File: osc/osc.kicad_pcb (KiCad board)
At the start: 2 copper layers, 25.4 x 25.4 mm, 18 parts, among them P1 CONN_1, P2 CONN_1, P3 CONN_1, P4 CONN_1, P5 CONN_1, P6 CONN_5X2, Y4 M100

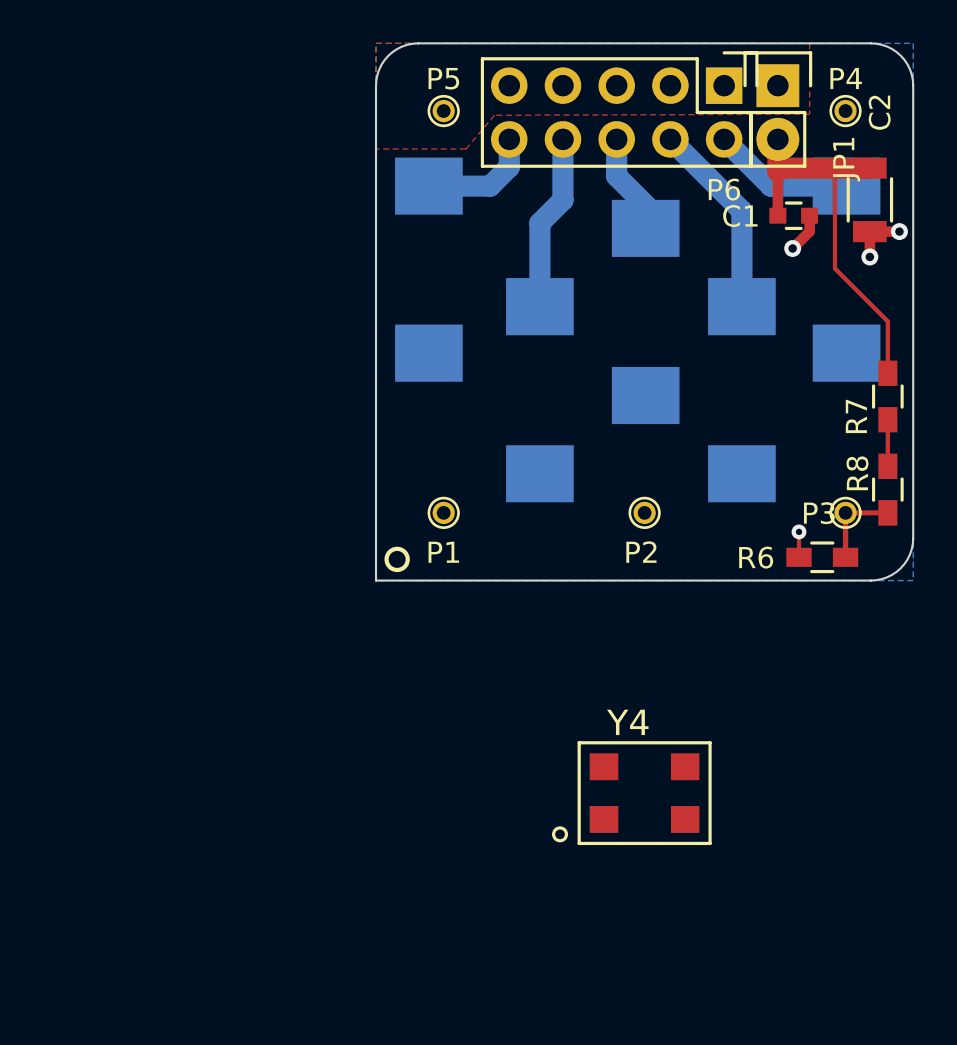
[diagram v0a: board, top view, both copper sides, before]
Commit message: Add Y3 footprint: SMT XO 7.0 x 5.0 mm
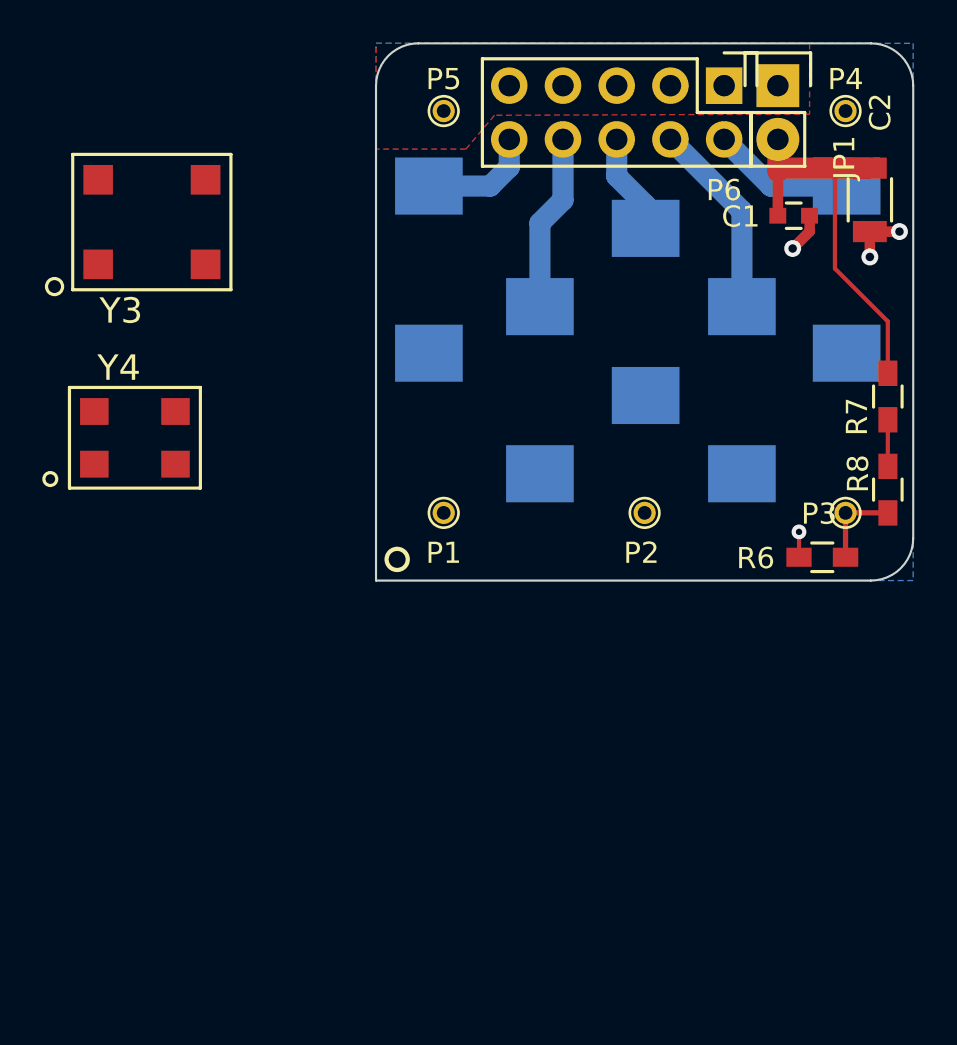
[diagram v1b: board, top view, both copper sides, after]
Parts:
- added Y3: AST3TQ-28, footprints:OSC7050, F.Cu at (89.4, 83.0)
- moved Y4 29.4 mm to (88.6, 93.2)
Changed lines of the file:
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@@
 (kicad_pcb (version 4) (host pcbnew 4.0.2-stable)
   (general
-    (links 29)
-    (no_connects 18)
-    (area 99.949999 74.549999 125.450001 100.050001)
+    (links 33)
+    (no_connects 22)
+    (area 84.070861 74.549999 127.025 101.725)
     (thickness 1.6)
     (drawings 8)
     (tracks 34)
     (zones 0)
-    (modules 18)
+    (modules 19)
     (nets 13)
   )
@@
       (effects (font (size 1 1) (thickness 0.1)))
     )
-    (fp_text value 0 (at 0 1.9 90) (layer F.Fab)
+    (fp_text value 0 (at 0 1.9 90) (layer F.Fab) hide
       (effects (font (size 1 1) (thickness 0.15)))
     )
@@
   )
   (module footprints:OSC5032 (layer F.Cu)
-    (at 112.7 110.050001)
+    (at 88.6 93.25)
     (fp_text reference Y4 (at -0.75 -3.3 180) (layer F.SilkS)
       (effects (font (size 1.2 1.2) (thickness 0.15)))
@@
       (net 2 /GND))
   )
+  (module footprints:OSC7050 (layer F.Cu)
+    (at 89.4 83.05)
+    (fp_text reference Y3 (at -1.45 4.2 180) (layer F.SilkS)
+      (effects (font (size 1.2 1.2) (thickness 0.15)))
+    )
+    (fp_text value AST3TQ-28 (at 0 0) (layer F.Fab)
+      (effects (font (size 1.2 1.2) (thickness 0.15)))
+    )
+    (fp_circle (center -4.6 3.05) (end -4.25 3.2) (layer F.SilkS) (width 0.15))
+    (fp_line (start -3.74 -3.2) (end -3.74 3.2) (layer F.SilkS) (width 0.15))
+    (fp_line (start -3.74 3.2) (end 3.74 3.2) (layer F.SilkS) (width 0.15))
+    (fp_line (start 3.74 3.2) (end 3.74 -3.2) (layer F.SilkS) (width 0.15))
+    (fp_line (start 3.74 -3.2) (end -3.74 -3.2) (layer F.SilkS) (width 0.15))
+    (pad 4 smd rect (at -2.54 -2) (size 1.4 1.4) (layers F.Cu F.Paste F.Mask)
+      (net 1 /Vdd))
+    (pad 1 smd rect (at -2.54 2) (size 1.4 1.4) (layers F.Cu F.Paste F.Mask)
+      (net 12 /Vc))
+    (pad 3 smd rect (at 2.54 -2) (size 1.4 1.4) (layers F.Cu F.Paste F.Mask)
+      (net 4 /Fout))
+    (pad 2 smd rect (at 2.54 2) (size 1.4 1.4) (layers F.Cu F.Paste F.Mask)
+      (net 2 /GND))
+  )

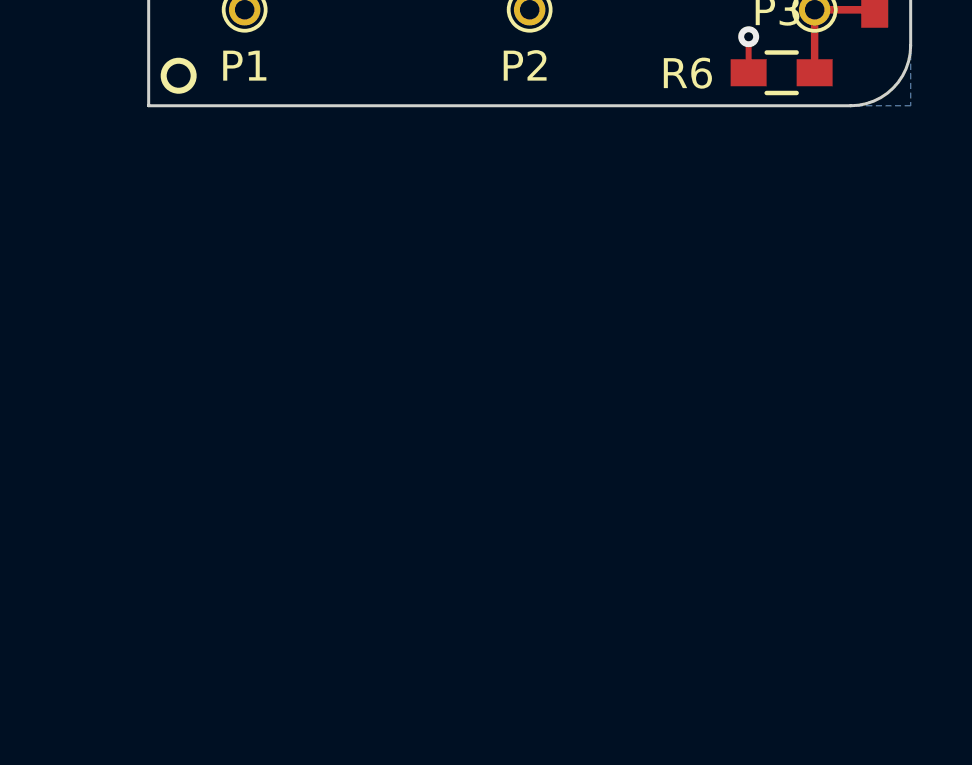
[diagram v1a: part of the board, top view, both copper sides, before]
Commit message: All footprints are created and added to the schematic and the board.
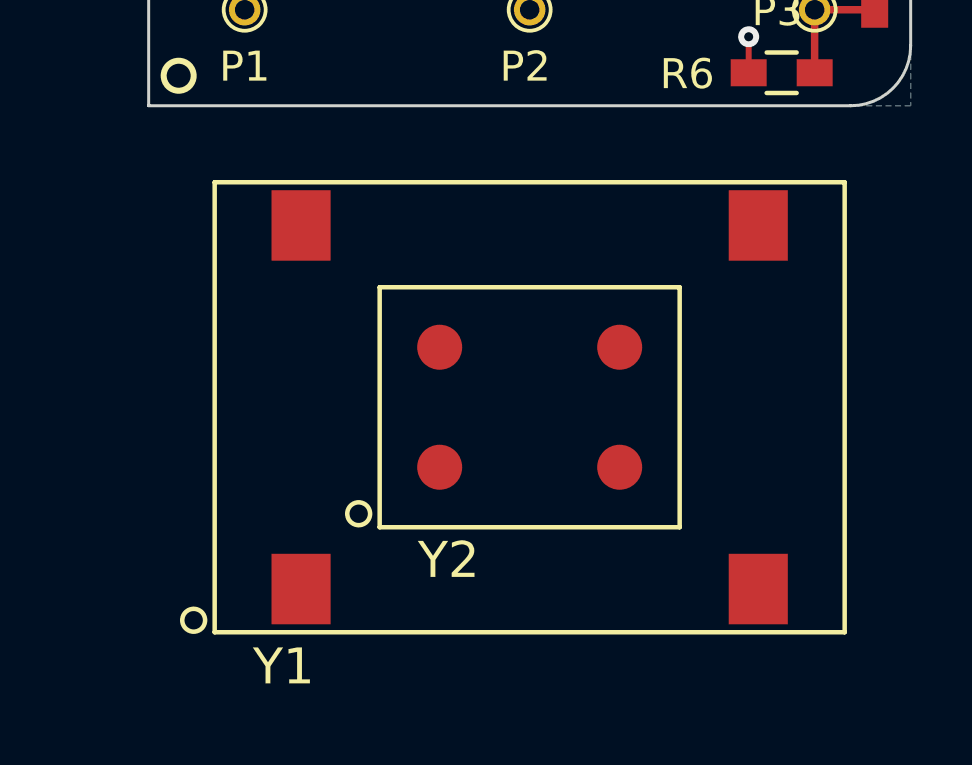
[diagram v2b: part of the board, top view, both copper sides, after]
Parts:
- added Y1: ASOF3S3, footprints:OSC-ASOF3S3, F.Cu at (112.7, 110.1)
- added Y2: AOCJYR, footprints:OSC-AOCJYR-SMT, F.Cu at (112.7, 110.1)
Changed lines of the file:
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@@
 (kicad_pcb (version 4) (host pcbnew 4.0.2-stable)
   (general
-    (links 33)
-    (no_connects 22)
-    (area 84.070861 74.549999 127.025 101.725)
+    (links 41)
+    (no_connects 30)
+    (area 84.070861 74.549999 127.025 119.765001)
     (thickness 1.6)
     (drawings 8)
     (tracks 34)
     (zones 0)
-    (modules 19)
+    (modules 21)
     (nets 13)
   )
@@
       (net 2 /GND))
   )
+  (module footprints:OSC-ASOF3S3 (layer F.Cu)
+    (at 112.7 110.050001)
+    (fp_text reference Y1 (at -8.2 8.65 180) (layer F.SilkS)
+      (effects (font (size 1.2 1.2) (thickness 0.15)))
+    )
+    (fp_text value ASOF3S3 (at 0 0) (layer F.Fab)
+      (effects (font (size 1.2 1.2) (thickness 0.15)))
+    )
+    (fp_circle (center -11.2 7.1) (end -10.85 7.25) (layer F.SilkS) (width 0.15))
+    (fp_line (start -10.5 -7.5) (end -10.5 7.5) (layer F.SilkS) (width 0.15))
+    (fp_line (start -10.5 7.5) (end 10.5 7.5) (layer F.SilkS) (width 0.15))
+    (fp_line (start 10.5 7.5) (end 10.5 -7.5) (layer F.SilkS) (width 0.15))
+    (fp_line (start 10.5 -7.5) (end -10.5 -7.5) (layer F.SilkS) (width 0.15))
+    (pad 14 smd rect (at -7.62 -6.06) (size 1.97 2.35) (layers F.Cu F.Paste F.Mask)
+      (net 1 /Vdd))
+    (pad 1 smd rect (at -7.62 6.06) (size 1.97 2.35) (layers F.Cu F.Paste F.Mask)
+      (net 12 /Vc))
+    (pad 8 smd rect (at 7.62 -6.06) (size 1.97 2.35) (layers F.Cu F.Paste F.Mask)
+      (net 4 /Fout))
+    (pad 7 smd rect (at 7.62 6.06) (size 1.97 2.35) (layers F.Cu F.Paste F.Mask)
+      (net 2 /GND))
+  )
+  (module footprints:OSC-AOCJYR-SMT (layer F.Cu)
+    (at 112.7 110.050001)
+    (fp_text reference Y2 (at -2.7 5.1) (layer F.SilkS)
+      (effects (font (size 1.2 1.2) (thickness 0.15)))
+    )
+    (fp_text value AOCJYR (at 0 0) (layer F.Fab)
+      (effects (font (size 1.2 1.2) (thickness 0.15)))
+    )
+    (fp_circle (center -5.7 3.55) (end -5.35 3.7) (layer F.SilkS) (width 0.15))
+    (fp_line (start -5 -4) (end -5 4) (layer F.SilkS) (width 0.15))
+    (fp_line (start -5 4) (end 5 4) (layer F.SilkS) (width 0.15))
+    (fp_line (start 5 4) (end 5 -4) (layer F.SilkS) (width 0.15))
+    (fp_line (start 5 -4) (end -5 -4) (layer F.SilkS) (width 0.15))
+    (pad 4 smd circle (at -3 -2) (size 1.5 1.5) (layers F.Cu F.Paste F.Mask)
+      (net 1 /Vdd))
+    (pad 1 smd circle (at -3 2) (size 1.5 1.5) (layers F.Cu F.Paste F.Mask)
+      (net 12 /Vc))
+    (pad 3 smd circle (at 3 -2) (size 1.5 1.5) (layers F.Cu F.Paste F.Mask)
+      (net 4 /Fout))
+    (pad 2 smd circle (at 3 2) (size 1.5 1.5) (layers F.Cu F.Paste F.Mask)
+      (net 2 /GND))
+  )

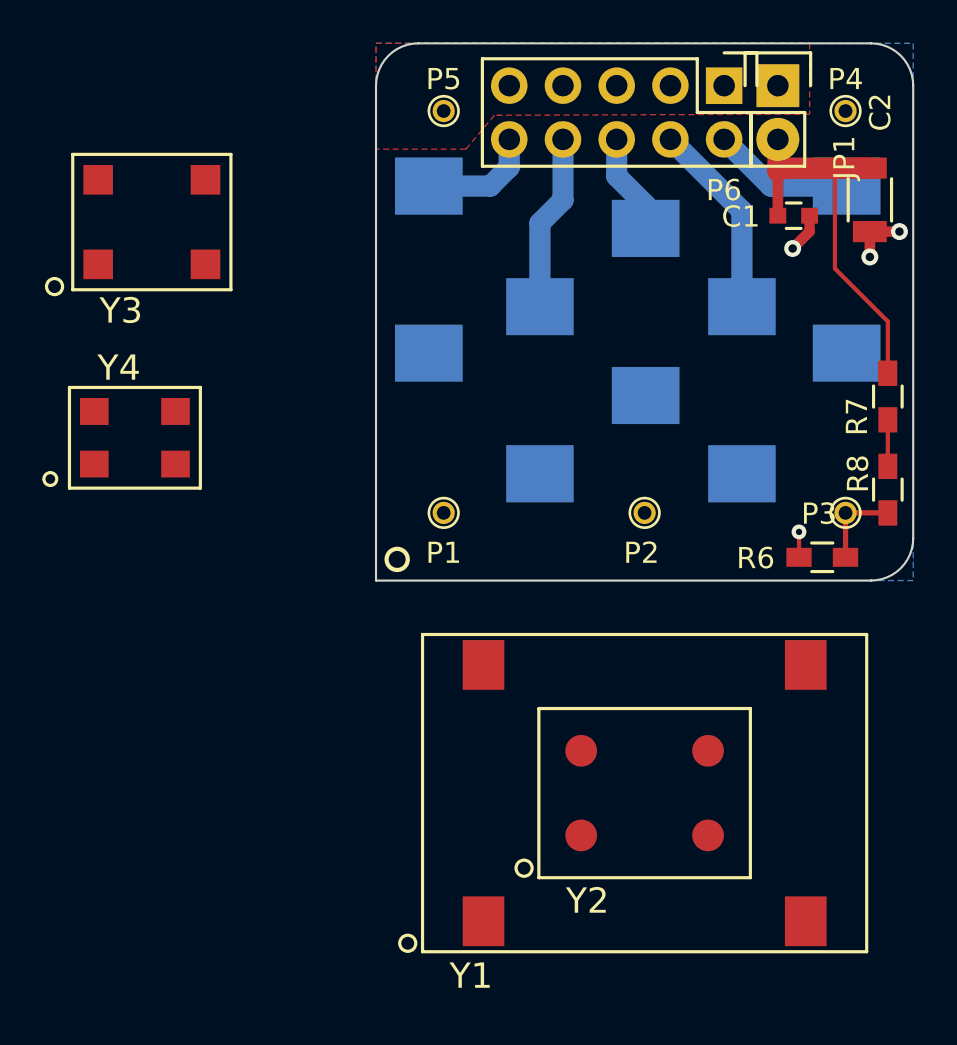
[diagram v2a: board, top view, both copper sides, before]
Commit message: Add an extra .1uF cap (build-time option, depends on the Osc assembled)
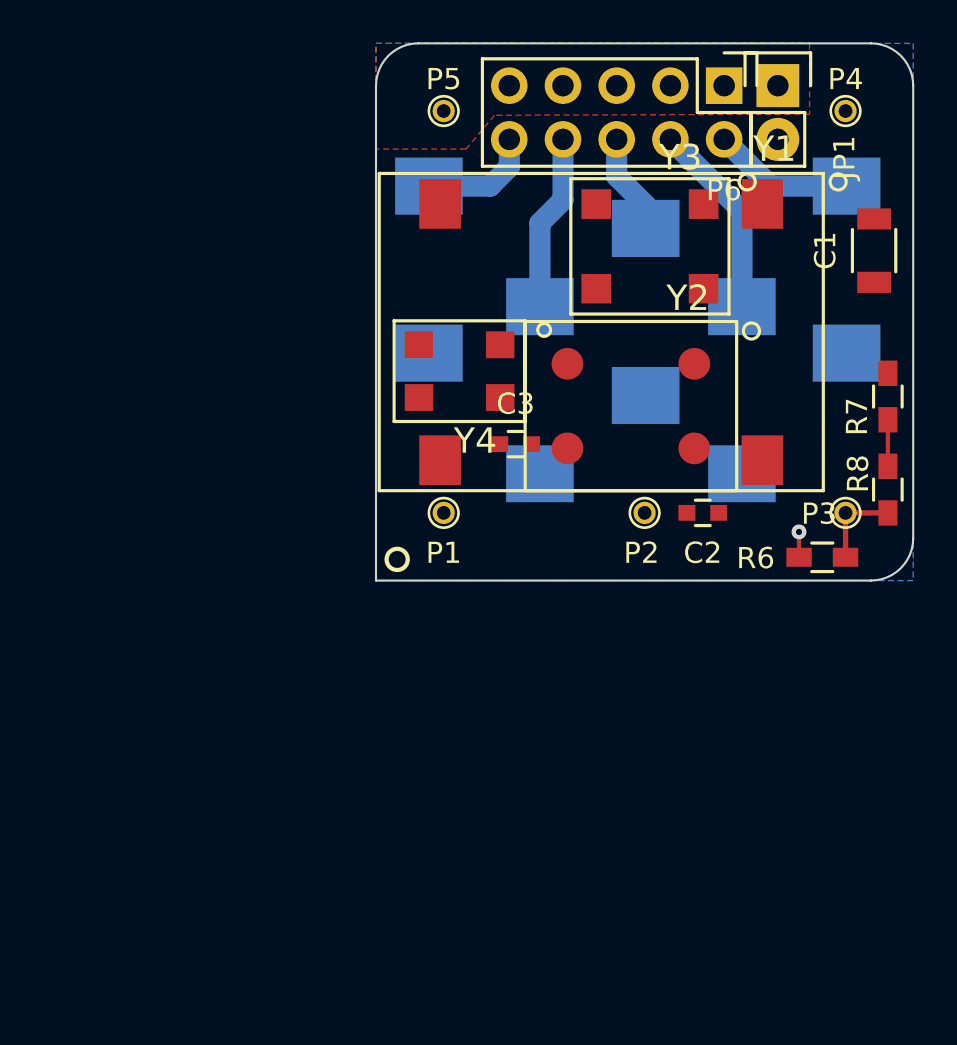
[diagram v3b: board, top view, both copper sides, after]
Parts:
- added C3: 0.1uF, Capacitors_SMD:C_0603, F.Cu at (106.6, 93.5)
- C1: value 0.1uF -> 10uF; footprint Capacitors_SMD:C_0603 -> Capacitors_SMD:C_1206
- C2: value 10uF -> 0.1uF; footprint Capacitors_SMD:C_1206 -> Capacitors_SMD:C_0603
- moved Y3 23.6 mm to (113.0, 84.2), turned to 180 degrees
- moved Y1 21.9 mm to (110.7, 88.2), turned to 180 degrees
- moved Y2 18.3 mm to (112.0, 91.8), turned to 180 degrees
- moved C2 16.8 mm to (115.5, 96.8), turned to 180 degrees
- moved Y4 15.7 mm to (104.0, 90.1), turned to 180 degrees
- moved C1 4.14 mm to (123.5, 84.4), turned to 90 degrees
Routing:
- net /Vdd: track 18.9 -> 0.00 mm
- net /GND: track 5.68 -> 1.20 mm, vias 4 -> 1
- net /Fout: track 0.00 -> 1.48 mm

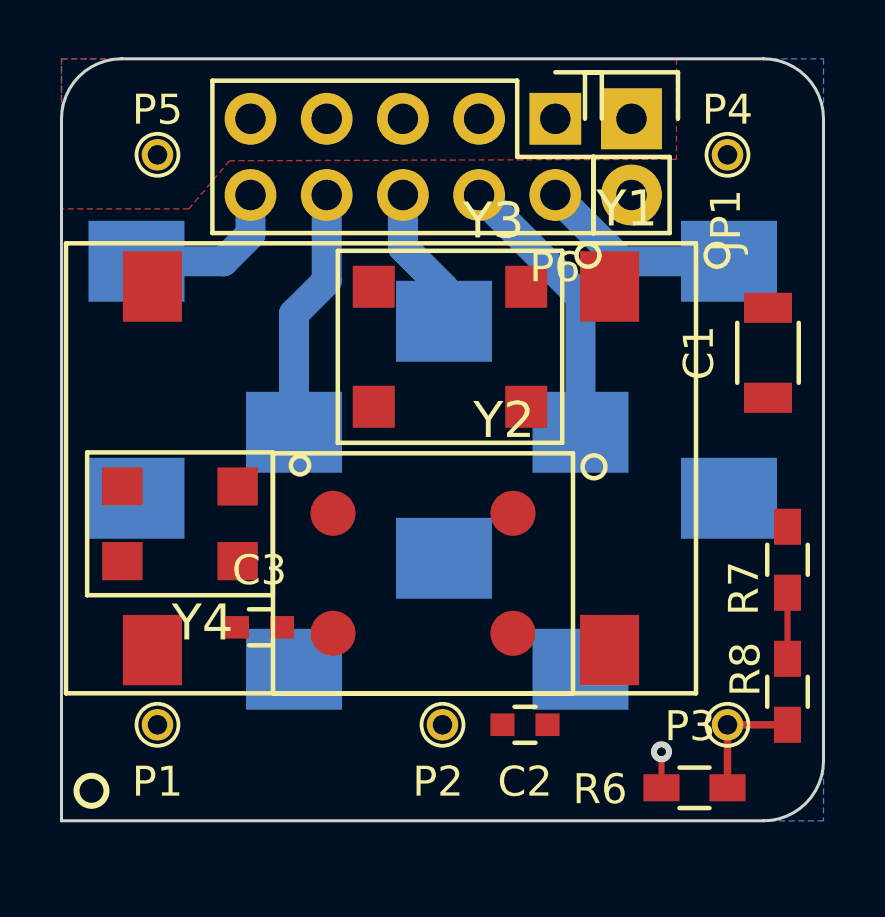
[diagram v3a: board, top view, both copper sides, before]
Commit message: Initial routing of all the signals (except ground connections)
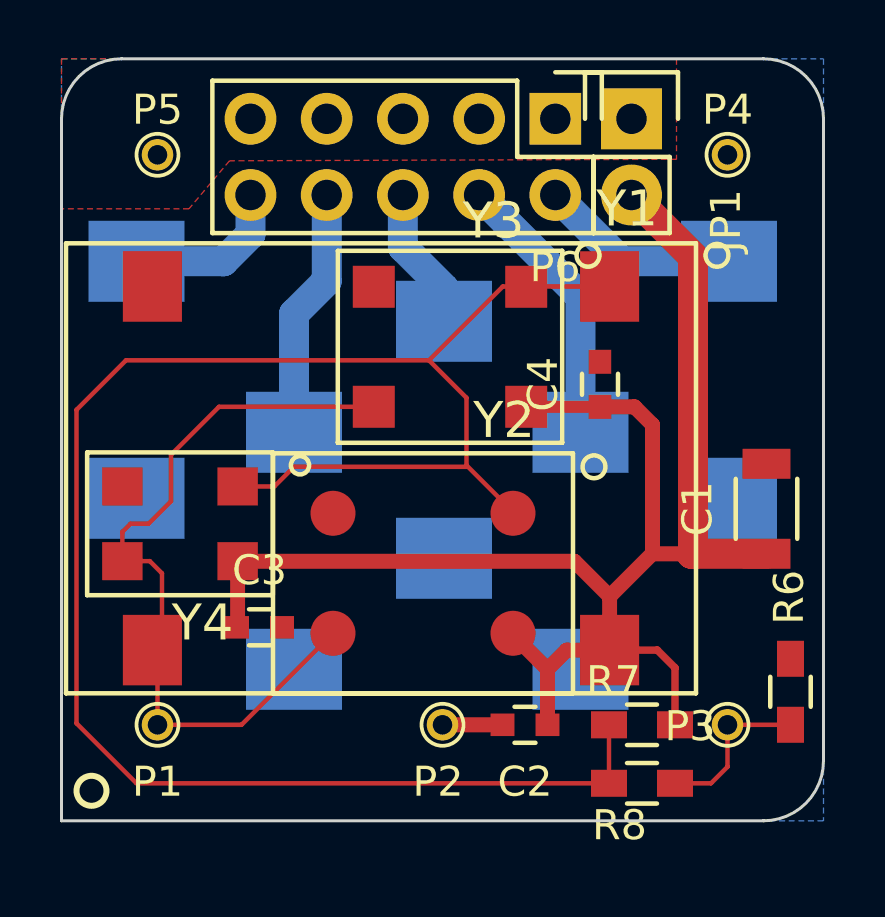
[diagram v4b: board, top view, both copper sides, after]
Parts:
- added C4: 0.1uF, Capacitors_SMD:C_0603, F.Cu at (118.0, 85.5)
- moved R7 7.33 mm to (119.3, 96.8), turned to 0 degrees
- moved R8 5.73 mm to (119.3, 98.8), turned to 180 degrees
- moved C1 5.20 mm to (123.5, 89.6)
- moved R6 4.53 mm to (124.3, 95.7), turned to 270 degrees
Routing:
- net /Vc: track 2.20 -> 64.7 mm
- net /Vdd: track 0.00 -> 54.6 mm
- net /Fout: track 1.48 -> 27.2 mm
- net Net-(P3-Pad1): track 4.10 -> 5.48 mm
- net /GND: track 1.20 -> 2.00 mm, vias 1 -> 0
